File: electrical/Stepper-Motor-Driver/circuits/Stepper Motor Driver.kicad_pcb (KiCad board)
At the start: 4 copper layers, 148 parts, among them J1 Screw_Terminal_01x03, J2 Screw_Terminal_01x04, Q1 IRF530NPBF, Q2 IRF530NPBF, Q3 IRF530NPBF, Q4 IRF530NPBF, Q5 IRF530NPBF, Q6 IRF530NPBF, Q7 IRF530NPBF, Q8 IRF530NPBF, U10 LM1117-Q1, U11 TPS54202DDC, U12 REF2033, U2 UCC27710D, U3 UCC27710D, U4 UCC27710D, U5 UCC27710D, U6 INA240A2PW, U7 ADS7042xDCU, U8 INA240A2PW, U9 ADS7042xDCU

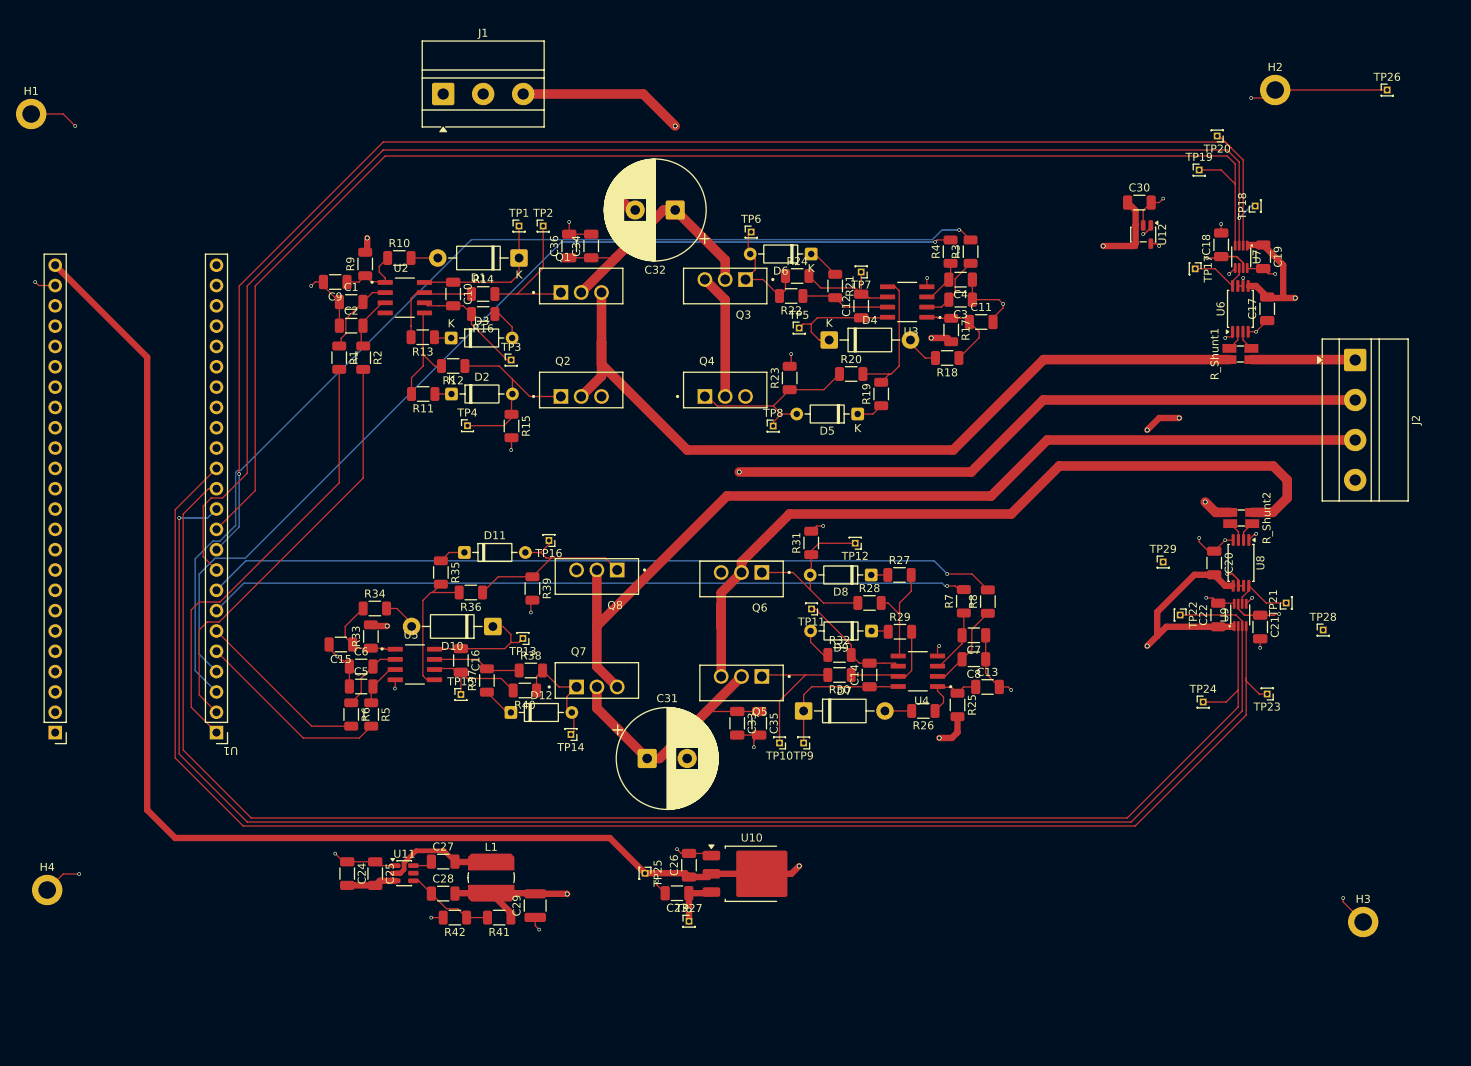
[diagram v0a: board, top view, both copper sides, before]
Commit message: Fixing via sizes and adding second ground plane below analog section
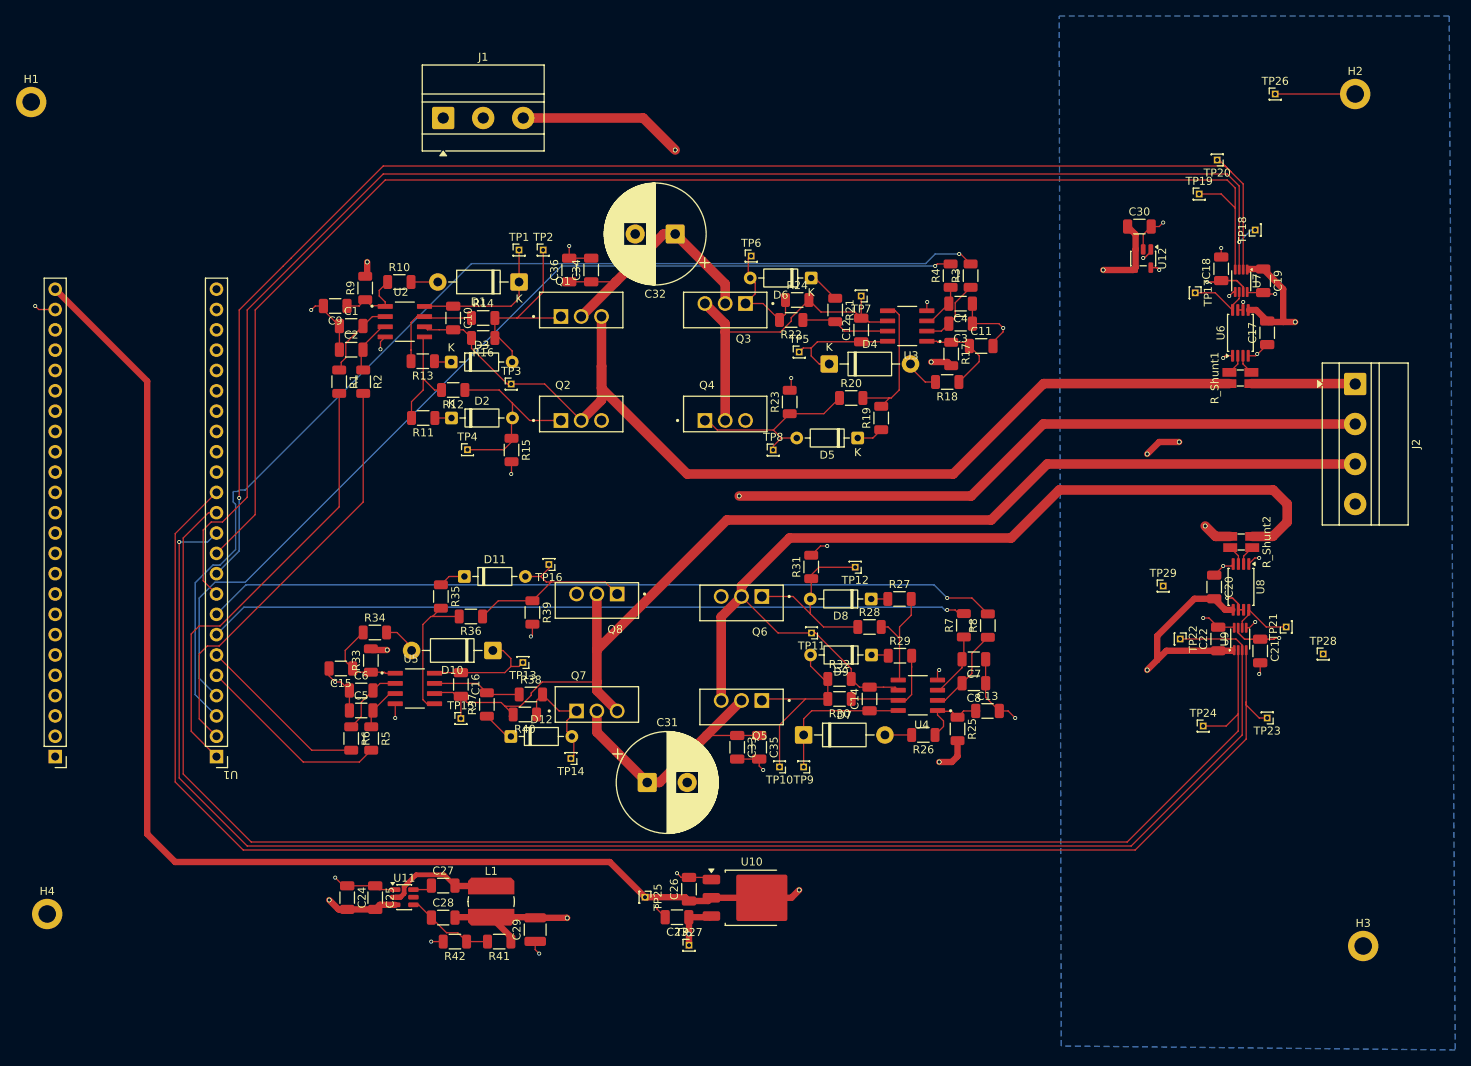
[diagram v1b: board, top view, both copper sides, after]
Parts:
- moved TP26 14.0 mm to (268.0, 15.5)
- moved H2 10.0 mm to (278.0, 15.5)
- moved C1 3.00 mm to (152.5, 44.5)
- moved C10 3.00 mm to (165.2, 43.5)
- moved C11 3.00 mm to (231.2, 47.0)
- moved C12 3.00 mm to (216.2, 45.0)
- moved C13 3.00 mm to (232.0, 92.6)
- moved C14 3.00 mm to (217.3, 91.1)
- moved C15 3.00 mm to (151.2, 87.3)
- moved C16 3.00 mm to (166.2, 89.3)
- moved C17 3.00 mm to (267.0, 45.4)
- moved C18 3.00 mm to (261.2, 37.4)
- moved C19 3.00 mm to (266.5, 38.9)
- moved C2 3.00 mm to (152.5, 47.5)
- moved C20 3.00 mm to (260.4, 77.1)
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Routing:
- net +12V: track 220.6 -> 258.4 mm, vias 4 -> 5
- net GND: track 137.7 -> 116.9 mm, vias 36 -> 31
- net /H-Bridge Controller B/BR2: track 134.5 -> 147.4 mm
- net /H-Bridge Controller A/BR2: track 121.0 -> 133.3 mm
- net /Current Sensor A/IN+: track 119.0 -> 129.6 mm
- net /Current Sensor B/IN+: track 114.0 -> 121.8 mm
- net Net-(D9-A): track 23.0 -> 25.5 mm
- net Net-(D3-A): track 23.0 -> 25.5 mm
- net +5V: track 181.0 -> 179.7 mm
- net /HI2A: track 136.1 -> 136.8 mm
- added copper zone on B.Cu, net GND

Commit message: Via cleanup
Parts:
- moved TP21 1.42 mm to (269.8, 80.8)
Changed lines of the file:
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@@
 	(footprint "Connector_PinHeader_1.00mm:PinHeader_1x01_P1.00mm_Vertical"
 		(layer "F.Cu")
-		(at 269.375001 82.12196 90)
+		(at 269.75 80.75 90)
 		(descr "Through hole straight pin header, 1x01, 1.00mm pitch, single row")
 		(tags "Through hole pin header THT 1x01 1.00mm single row")
@@
 	)
 	(segment
-		(start 262.663157 78.5)
+		(start 261.161276 77)
+		(end 258 77)
+		(width 0.2)
+		(layer "F.Cu")
+		(net "+1.65V-REF")
+	)
+	(segment
+		(start 263.400657 79.975)
 		(end 263.400657 79.2375)
 		(width 0.2)
@@
 	)
 	(segment
-		(start 262 78.5)
-		(end 262.663157 78.5)
+		(start 262.661276 78.5)
+		(end 261.161276 77)
+		(width 0.2)
+		(layer "F.Cu")
+		(net "+1.65V-REF")
+	)
+	(segment
+		(start 262.663157 78.5)
+		(end 262.661276 78.5)
 		(width 0.2)
 		(layer "F.Cu")
@@
 	)
 	(segment
-		(start 252.45 35.211616)
-		(end 252.45 34.93125)
+		(start 263.400657 79.2375)
+		(end 262.663157 78.5)
 		(width 0.2)
 		(layer "F.Cu")
@@
 	)
 	(segment
-		(start 263.400657 79.2375)
-		(end 263.400657 79.975)
+		(start 252.45 35.211616)
+		(end 252.45 34.93125)
 		(width 0.2)
 		(layer "F.Cu")
@@
 	)
 	(via
-		(at 262 78.5)
+		(at 258 77)
 		(size 0.5)
 		(drill 0.3)
@@
 	)
 	(segment
-		(start 260.5 77)
-		(end 262 78.5)
-		(width 0.2)
-		(layer "In2.Cu")
-		(net "+1.65V-REF")
-	)
-	(segment
 		(start 251.5 39)
 		(end 251.5 36)
@@
 	)
 	(segment
-		(start 258 77)
-		(end 260.5 77)
-		(width 0.2)
-		(layer "In2.Cu")
-		(net "+1.65V-REF")
-	)
-	(segment
 		(start 254 73)
 		(end 258 77)
@@
 	)
 	(segment
-		(start 267.85304 83.64696)
-		(end 266.125001 83.64696)
+		(start 259.5 39)
+		(end 261.075 39)
 		(width 0.2)
 		(layer "F.Cu")
@@
 	)
 	(segment
-		(start 268.5 83.5)
+		(start 271.5 83.5)
 		(end 268 83.5)
 		(width 0.2)
@@
 	)
 	(segment
-		(start 268 83.5)
-		(end 267.85304 83.64696)
-		(width 0.2)
-		(layer "F.Cu")
-		(net "+3.3V-REF")
-	)
-	(segment
-		(start 259.5 39)
-		(end 261.075 39)
+		(start 264.175002 83.64696)
+		(end 266.125001 83.64696)
 		(width 0.2)
 		(layer "F.Cu")
@@
 	)
 	(segment
-		(start 264.175002 83.64696)
+		(start 267.85304 83.64696)
 		(end 266.125001 83.64696)
 		(width 0.2)
@@
 		(net "+3.3V-REF")
 	)
+	(segment
+		(start 268 83.5)
+		(end 267.85304 83.64696)
+		(width 0.2)
+		(layer "F.Cu")
+		(net "+3.3V-REF")
+	)
 	(via
 		(at 259.5 39)
@@
 	)
 	(via
-		(at 268.5 83.5)
+		(at 271.5 83.5)
 		(size 0.5)
 		(drill 0.3)
@@
 	)
 	(segment
-		(start 274 83.5)
-		(end 268.5 83.5)
-		(width 0.2)
-		(layer "In2.Cu")
-		(net "+3.3V-REF")
-	)
-	(segment
 		(start 258 37.5)
 		(end 259.5 39)
@@
 	)
 	(segment
+		(start 274 83.5)
+		(end 271.5 83.5)
+		(width 0.2)
+		(layer "In2.Cu")
+		(net "+3.3V-REF")
+	)
+	(segment
 		(start 199.25 41.69)
 		(end 199.25 39.25)
@@
 	)
 	(segment
-		(start 264.600001 80.673002)
-		(end 264.600001 80.075656)
+		(start 265.503041 80.75)
+		(end 269.75 80.75)
 		(width 0.15)
 		(layer "F.Cu")
@@
 	)
 	(segment
-		(start 264.600001 80.075656)
-		(end 264.700657 79.975)
+		(start 264.737501 79.98446)
+		(end 265.503041 80.75)
 		(width 0.15)
 		(layer "F.Cu")
@@
 	)
 	(segment
-		(start 263.875001 82.22196)
-		(end 263.875001 81.398002)
+		(start 264.600001 80.673002)
+		(end 264.600001 80.075656)
 		(width 0.15)
 		(layer "F.Cu")
@@
 	)
 	(segment
-		(start 264.710117 79.98446)
-		(end 264.737501 79.98446)
+		(start 264.600001 80.075656)
+		(end 264.700657 79.975)
 		(width 0.15)
 		(layer "F.Cu")
@@
 	)
 	(segment
-		(start 264.737501 79.98446)
-		(end 266.875001 82.12196)
+		(start 263.875001 82.22196)
+		(end 263.875001 81.398002)
 		(width 0.15)
 		(layer "F.Cu")
@@
 	)
 	(segment
-		(start 264.700657 79.975)
-		(end 264.710117 79.98446)
+		(start 264.710117 79.98446)
+		(end 264.737501 79.98446)
 		(width 0.15)
 		(layer "F.Cu")
@@
 	)
 	(segment
-		(start 266.875001 82.12196)
-		(end 269.375001 82.12196)
+		(start 264.700657 79.975)
+		(end 264.710117 79.98446)
 		(width 0.15)
 		(layer "F.Cu")
@@
 	)
 	(segment
-		(start 133.5 85.5)
-		(end 133.5 93.62)
+		(start 136 84.5)
+		(end 134.5 84.5)
 		(width 0.15)
 		(layer "F.Cu")
@@
 	)
 	(segment
-		(start 134.5 84.5)
-		(end 133.5 85.5)
+		(start 154 52.925)
+		(end 154 66.5)
 		(width 0.15)
 		(layer "F.Cu")
@@
 	)
 	(segment
-		(start 133.5 93.62)
-		(end 135.66 95.78)
+		(start 133.25 85.75)
+		(end 133.25 93.37)
 		(width 0.15)
 		(layer "F.Cu")
@@
 	)
 	(segment
-		(start 136 84.5)
-		(end 134.5 84.5)
+		(start 134.5 84.5)
+		(end 133.25 85.75)
 		(width 0.15)
 		(layer "F.Cu")
@@
 	)
 	(segment
-		(start 154 52.925)
-		(end 154 66.5)
+		(start 133.25 93.37)
+		(end 135.66 95.78)
 		(width 0.15)
 		(layer "F.Cu")

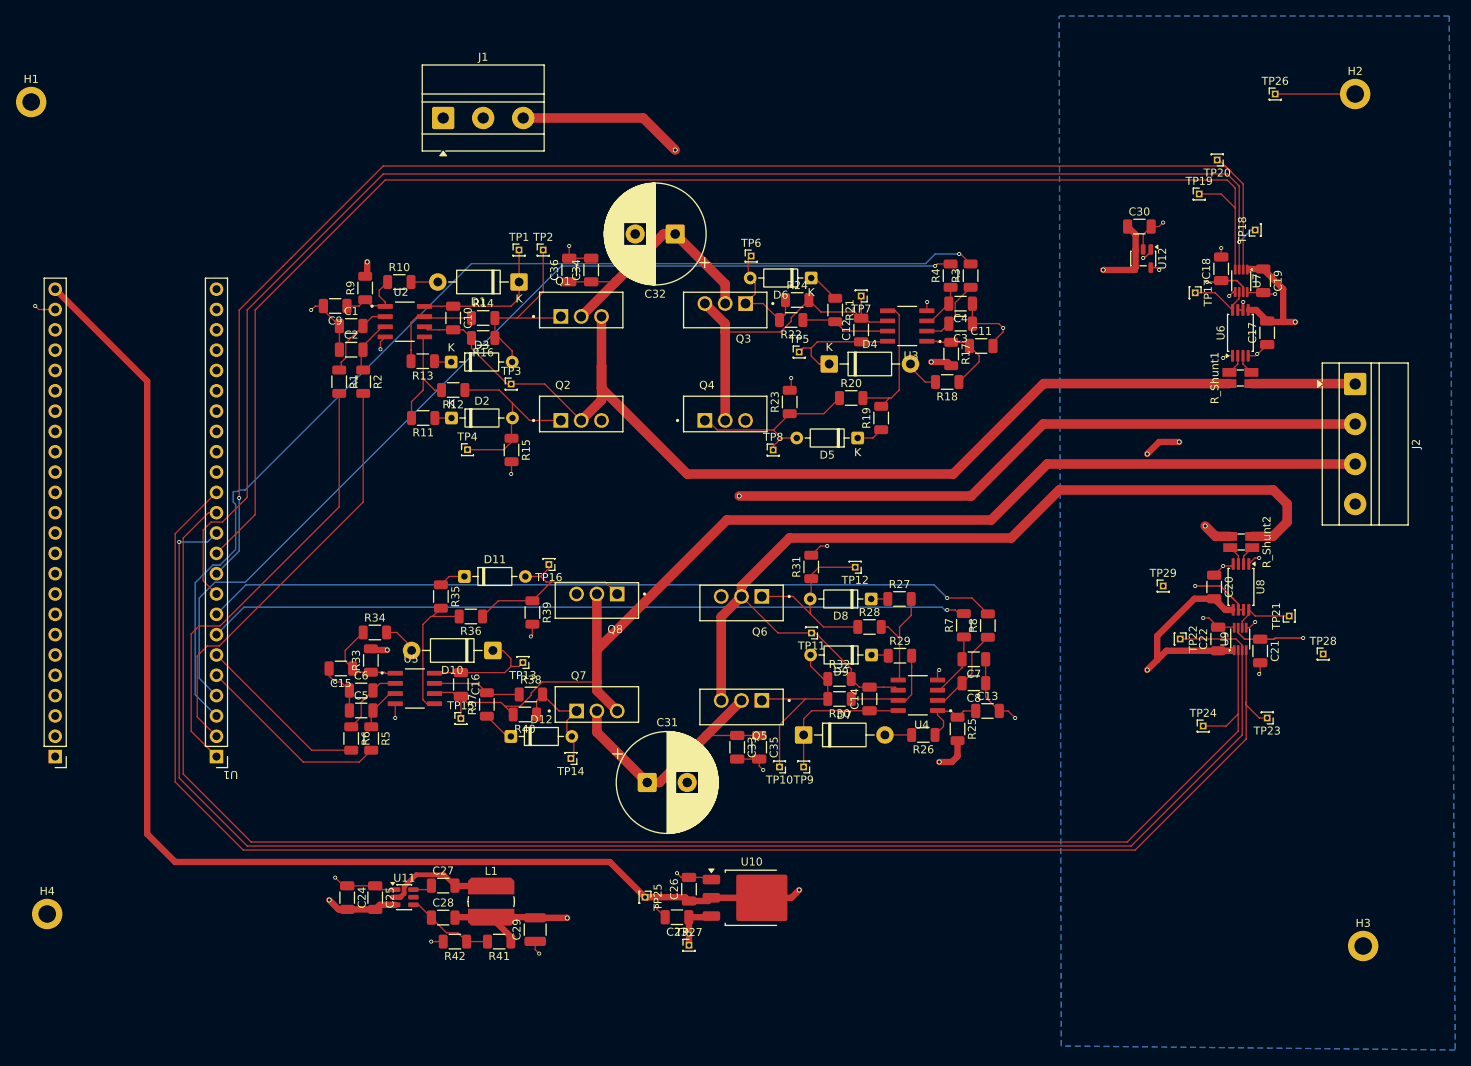
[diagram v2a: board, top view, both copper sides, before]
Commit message: Redoing FPGA pin assignment to optimize signal trace lengths
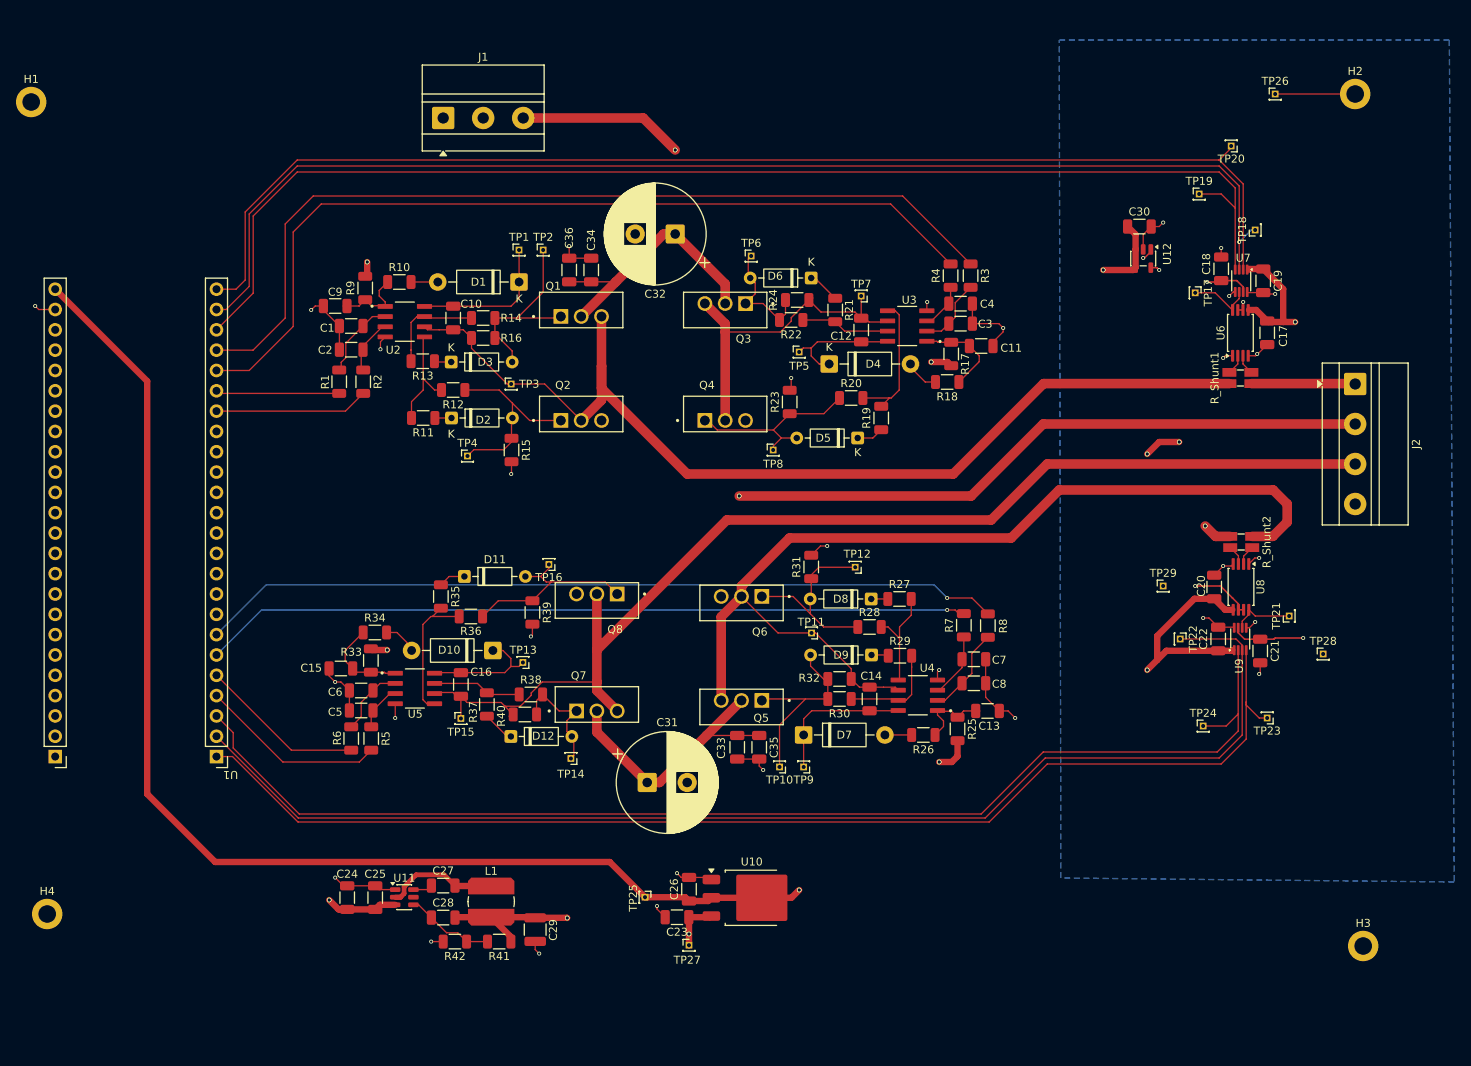
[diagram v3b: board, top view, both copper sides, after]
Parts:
- moved TP20 2.47 mm to (262.5, 22.0)
- moved TP4 0.79 mm to (167.0, 60.8)
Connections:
- U1 pad 25: /LI2B -> /HI2B
- U1 pad 26: /HI2B -> /LI1B
- U1 pad 27: /LI1B -> /HI1B
- U1 pad 28: /HI1B -> unconnected-(U1-IOB11B-Pad28)
- U1 pad 29: /SDOA -> unconnected-(U1-IOB13A-Pad29)
- U1 pad 30: /SCLKA -> unconnected-(U1-IOB13B-Pad30)
- U1 pad 33: /~{CS}A -> unconnected-(U1-IOB23A-Pad33)
- U1 pad 34: /SDOB -> unconnected-(U1-IOB23B-Pad34)
- U1 pad 35: /~{CS}B -> unconnected-(U1-IOB29A-Pad35)
- U1 pad 36: /HI2A -> /SCLKB
- U1 pad 37: /LI1A -> /SDOB
- U1 pad 38: /HI1A -> /~{CS}B
- U1 pad 39: /LI2A -> /LI2B
- U1 pad 40: /SCLKB -> unconnected-(U1-IOB33B-Pad40)
- U1 pad 53: unconnected-(U1-IOR15B-Pad53) -> /LI1A
- U1 pad 54: unconnected-(U1-IOR15A-Pad54) -> /HI1A
- U1 pad 55: unconnected-(U1-IOR14B-Pad55) -> /LI2A
- U1 pad 56: unconnected-(U1-IOR14A-Pad56) -> /HI2A
- U1 pad 57: unconnected-(U1-IOR13A-Pad57) -> /~{CS}A
- U1 pad 68: unconnected-(U1-IOT42B-Pad68) -> /SDOA
- U1 pad 69: unconnected-(U1-IOT42A-Pad69) -> /SCLKA
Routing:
- net /~{CS}B: track 196.3 -> 151.2 mm
- net /HI1A: track 55.9 -> 15.5 mm
- net /SDOB: track 196.1 -> 156.0 mm, vias 1 -> 0
- net /SCLKB: track 191.2 -> 153.3 mm
- net /LI1A: track 53.3 -> 19.3 mm
- net /SDOA: track 184.0 -> 154.7 mm
- net /SCLKA: track 180.9 -> 154.3 mm, vias 1 -> 0
- net /HI2A: track 136.8 -> 112.6 mm, vias 1 -> 0
- net /~{CS}A: track 177.5 -> 157.4 mm
- net /LI2A: track 124.3 -> 110.4 mm, vias 1 -> 0
- net +3.3V: track 316.8 -> 313.9 mm
- net /LI2B: track 24.4 -> 23.4 mm
- net /HI1B: track 99.5 -> 100.5 mm
- net /HI2B: track 21.8 -> 20.7 mm
- net /LI1B: track 95.2 -> 95.9 mm

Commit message: Adding series termination resistors for high frequency digital signals
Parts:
- added R43: 50, Resistor_SMD:R_1206_3216Metric, F.Cu at (263.5, 32.0)
- added R44: 50, Resistor_SMD:R_1206_3216Metric, F.Cu at (264.0, 90.5)
- added R45: 50, Resistor_SMD:R_1206_3216Metric, F.Cu at (136.0, 34.5)
- added R46: 50, Resistor_SMD:R_1206_3216Metric, F.Cu at (141.5, 41.0)
- added R47: 50, Resistor_SMD:R_1206_3216Metric, F.Cu at (136.0, 103.5)
- added R48: 50, Resistor_SMD:R_1206_3216Metric, F.Cu at (140.5, 93.5)
- moved TP18 4.03 mm to (269.0, 34.5)
- moved TP23 1.50 mm to (268.5, 93.5)
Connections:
- TP18 pad 1: /SDOA -> /Current Sensor A/SDO
- TP22 pad 1: /SDOB -> /Current Sensor B/SDO
- U1 pad 36: /SCLKB -> Net-(U1-IOB29B)
- U1 pad 38: /~{CS}B -> Net-(U1-IOB31B)
- U1 pad 57: /~{CS}A -> Net-(U1-IOR13A)
- U1 pad 69: /SCLKA -> Net-(U1-IOT42A)
- U7 pad 3: /SDOA -> /Current Sensor A/SDO
- U9 pad 3: /SDOB -> /Current Sensor B/SDO
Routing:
- net /SDOB: track 156.0 -> 140.8 mm
- net /Current Sensor B/SDO: track 0.00 -> 12.1 mm
- net /Current Sensor A/SDO: track 0.00 -> 9.90 mm, vias 0 -> 1
- net /SDOA: track 154.7 -> 145.1 mm, vias 1 -> 0
- net /~{CS}A: track 157.4 -> 149.2 mm
- net Net-(U1-IOR13A): track 0.00 -> 8.09 mm
- net /SCLKA: track 154.3 -> 147.0 mm
- net /SCLKB: track 153.3 -> 148.5 mm
- net Net-(U1-IOT42A): track 0.00 -> 4.08 mm
- net Net-(U1-IOB31B): track 0.00 -> 3.86 mm
- net Net-(U1-IOB29B): track 0.00 -> 3.49 mm
- net /~{CS}B: track 151.2 -> 149.0 mm

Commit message: Adding missing decoupling for FPGA 3.3V
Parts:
- added C37: 100nF, Capacitor_SMD:C_1206_3216Metric, F.Cu at (119.0, 41.0)
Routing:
- net GND: track 116.9 -> 120.0 mm
- net +3.3V: track 313.9 -> 316.4 mm
